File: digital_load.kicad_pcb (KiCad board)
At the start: 2 copper layers, 100 x 95 mm, 77 parts, among them J1 Conn_01x02, J10 Conn_PIC_ICSP_ICD, J2 Conn_01x02, J3 Conn_01x04, J4 Conn_01x04, J5 USB_C_Receptacle_USB2.0, Q20 BSB280N15NZ3, Q21 Q_NMOS_DGS, Q22 Q_NMOS_DGS, Q23 Q_NMOS_DGS, SW30 PEC11R, U10 PIC18F24K42, U20 LM358, U21 LM4040DBZ-2.0, U30 Adafruit_PiOLED, U40 LP2951-3.3_SOIC, U60 FT232RL, U61 CP2102N-Axx-xQFN28, U62 CH340C

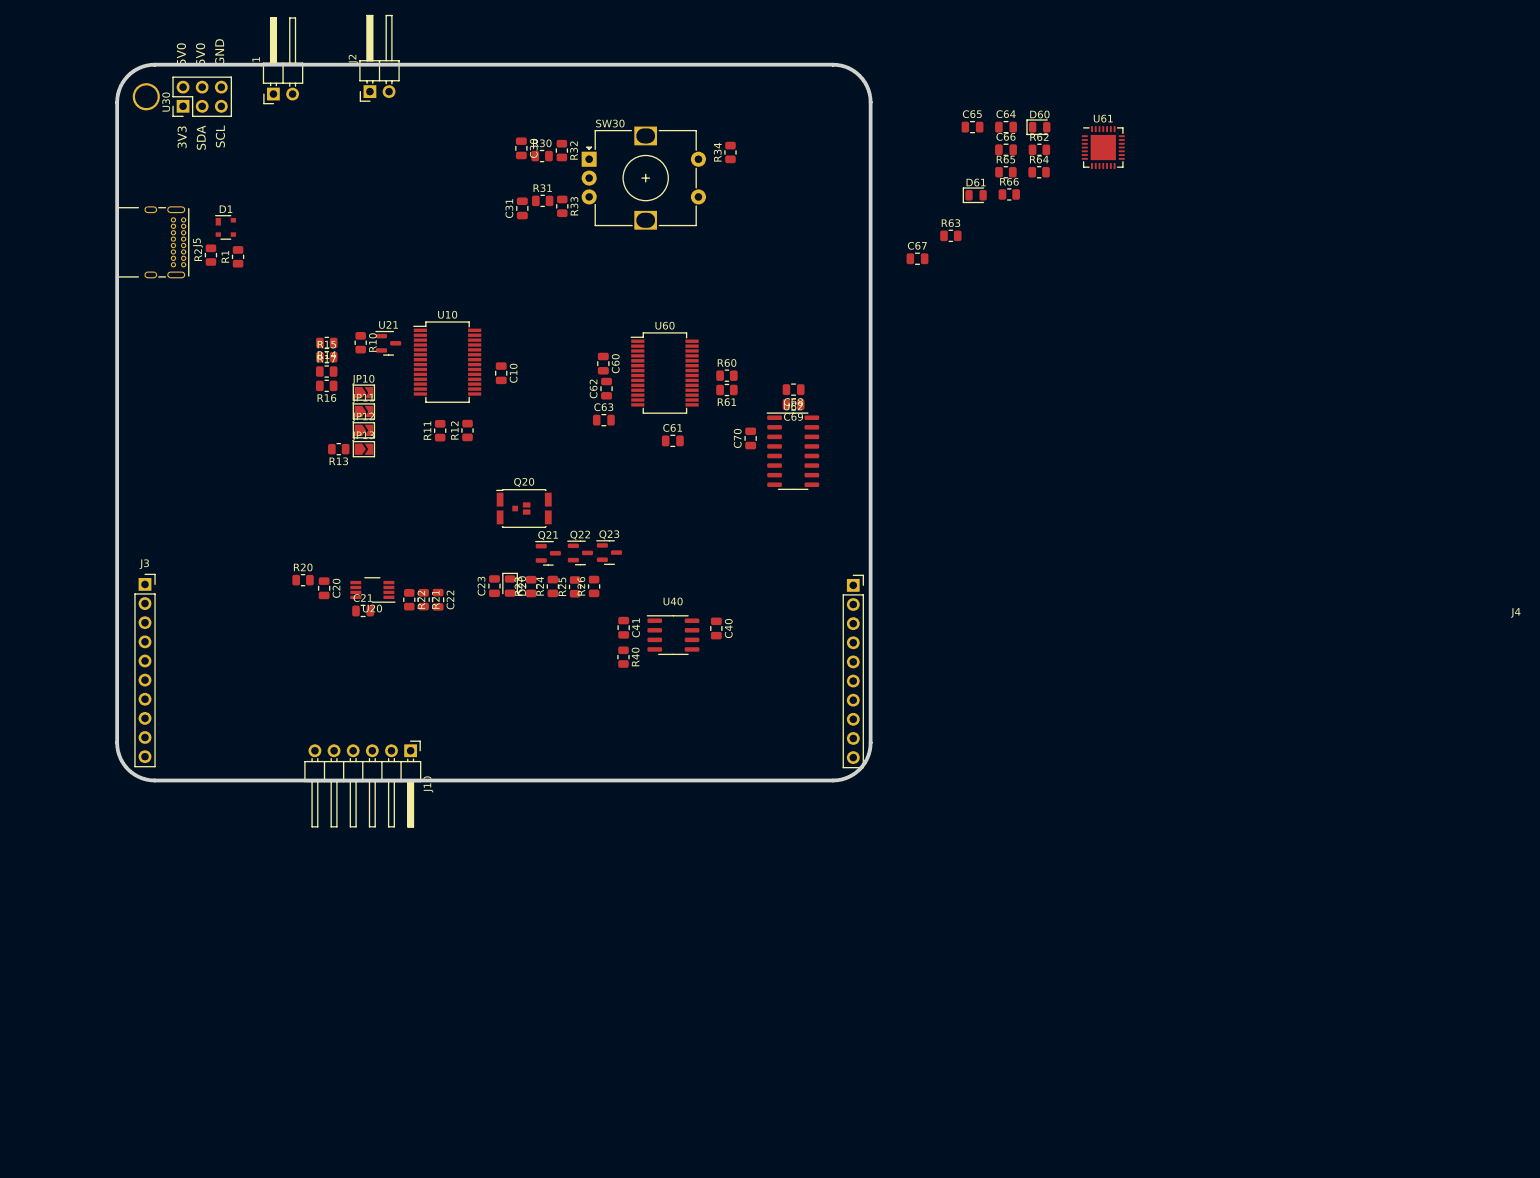
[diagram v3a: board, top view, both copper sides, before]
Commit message: WIP PCB Routing + Add load voltage measure
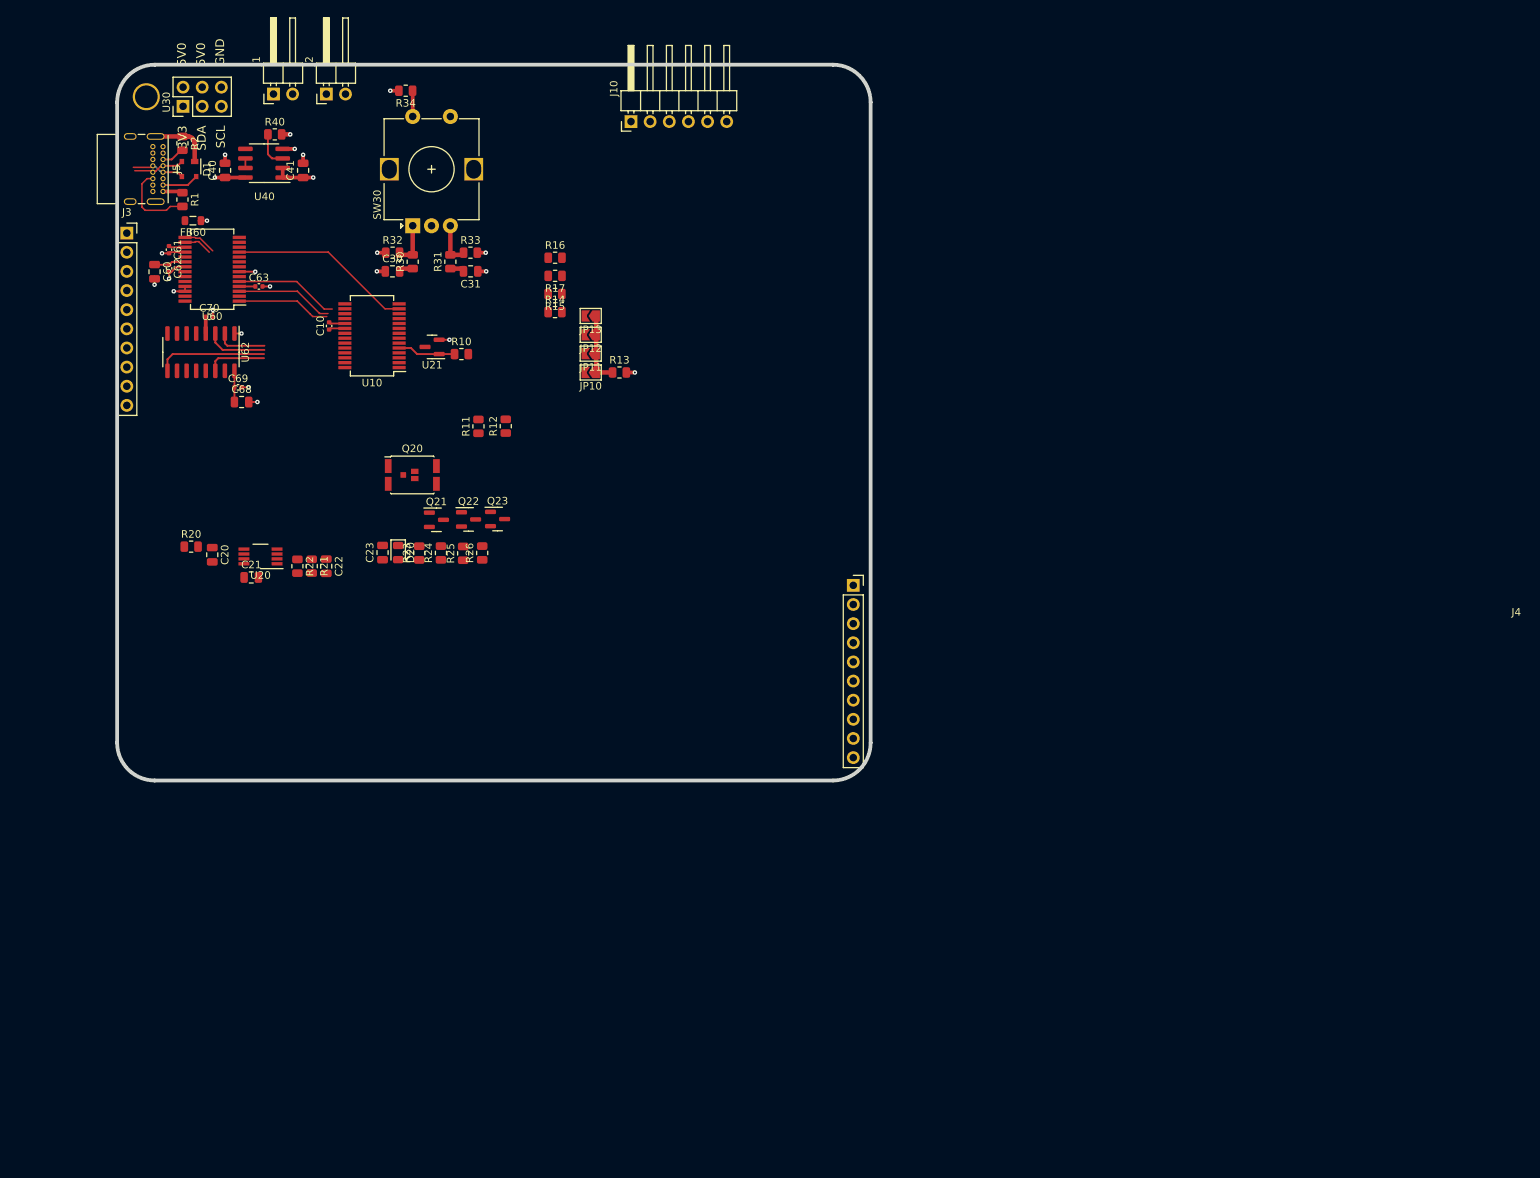
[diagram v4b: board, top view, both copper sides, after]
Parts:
- removed C64, C65: 100n, Capacitor_SMD:C_0805_2012Metric
- removed C66, C67: 4.7u, Capacitor_SMD:C_0805_2012Metric
- removed D60, D61: LED, LED_SMD:LED_0805_2012Metric
- removed R60: 4.7k, Resistor_SMD:R_0805_2012Metric
- removed R61, R65, R66: 10k, Resistor_SMD:R_0805_2012Metric
- removed R62: 22.1k, Resistor_SMD:R_0805_2012Metric
- removed R63: 47.5k, Resistor_SMD:R_0805_2012Metric
- removed R64: 1k, Resistor_SMD:R_0805_2012Metric
- removed U61: CP2102N-Axx-xQFN28, Package_DFN_QFN:QFN-28-1EP_5x5mm_P0.5mm_EP3.35x3.35mm
- added FB60: FerriteBead, Inductor_SMD:L_0805_2012Metric, F.Cu at (110.1, 55.7)
- C10, C61, C62, C63, C69, C70: footprint Capacitor_SMD:C_0805_2012Metric -> Capacitor_SMD:C_0402_1005Metric
- moved C40 89.1 mm to (114.3, 49.0), turned to 90 degrees
- moved J10 88.5 mm to (168.2, 42.5), turned to 90 degrees
- moved R40 83.4 mm to (120.9, 44.2), turned to 0 degrees
- moved U40 82.9 mm to (119.5, 48.1), turned to 180 degrees
- moved U62 79.7 mm to (111.1, 73.2), turned to -90 degrees
- moved C41 74.1 mm to (124.7, 49.0), turned to 90 degrees
- moved C69 73.8 mm to (116.0, 77.8), turned to 0 degrees
- moved C70 73.6 mm to (112.2, 68.5), turned to 0 degrees
- moved C68 73.3 mm to (116.5, 79.8), turned to 0 degrees
- moved C61 71.5 mm to (106.9, 59.5), turned to -90 degrees
- moved U60 61.6 mm to (112.6, 62.1), turned to 180 degrees
- moved C60 60.8 mm to (105.0, 62.5)
- moved C62 60.2 mm to (106.9, 62.0), turned to -90 degrees
- moved C63 49.1 mm to (118.8, 64.4)
- moved J3 46.7 mm to (101.3, 57.4)
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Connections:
- C60 pad 1: +5V -> Net-(C60-Pad1)
- C62 pad 1: +5V -> Net-(C60-Pad1)
- C63 pad 1: +5V -> Net-(C60-Pad1)
- U60 pad 19: Net-(R60-Pad1) -> unconnected-(U60-Pad19)
- U60 pad 20: +5V -> Net-(C60-Pad1)
- U60 pad 4: +5V -> Net-(C60-Pad1)
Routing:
- net /microcontroller/UART.RTS: track 0.00 -> 39.0 mm
- net GND: track 0.00 -> 38.1 mm, vias 0 -> 17
- net /microcontroller/UART.TX: track 0.00 -> 22.0 mm
- net /microcontroller/UART.CTS: track 0.00 -> 20.9 mm
- net /microcontroller/UART.RX: track 0.00 -> 19.1 mm
- net +5V: track 0.00 -> 14.2 mm, vias 0 -> 2
- net +3V3: track 0.00 -> 12.0 mm, vias 0 -> 5
- net /Connectors/USB2.0.D+: track 0.00 -> 11.3 mm
- net /Connectors/USB2.0.D-: track 0.00 -> 10.9 mm
- net Net-(J5-PadB5): track 0.00 -> 10.6 mm
- net Net-(JP10-Pad1): track 0.00 -> 9.68 mm
- net /microcontroller/2.048V: track 0.00 -> 7.70 mm
- net Net-(C60-Pad1): track 0.00 -> 5.95 mm
- net Net-(R31-Pad2): track 0.00 -> 5.74 mm
- net Net-(R30-Pad2): track 0.00 -> 5.73 mm
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- added copper zone on In1.Cu, net GND
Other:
- copper layers 2 -> 4
- rule pad_to_mask_clearance: 0 -> 0.1

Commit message: WIP PCB Routing
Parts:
- removed J2: Conn_01x02, Connector_PinHeader_2.54mm:PinHeader_1x02_P2.54mm_Horizontal
- added C24: 100n, Capacitor_SMD:C_0402_1005Metric, F.Cu at (112.6, 137.9)
- added R27: 5M, Resistor_SMD:R_0805_2012Metric, F.Cu at (117.2, 145.8)
- added R28: 50k, Resistor_SMD:R_0805_2012Metric, F.Cu at (112.8, 145.8)
- added R29: 10k, Resistor_SMD:R_0805_2012Metric, F.Cu at (115.9, 137.7)
- added U21: LM358, Package_SO:VSSOP-8_3.0x3.0mm_P0.65mm, F.Cu at (110.9, 140.7)
- C21: value C_Small -> 100n; footprint Capacitor_SMD:C_0805_2012Metric -> Capacitor_SMD:C_0402_1005Metric
- J10: footprint Connector_PinHeader_2.54mm:PinHeader_1x06_P2.54mm_Horizontal -> Connector_PinHeader_2.54mm:PinHeader_1x06_P2.54mm_Vertical
- JP10, JP11, JP12, JP13: value SolderJumper_2_Open -> SB
- Q20: value BSB280N15NZ3 -> IPA60R800CE; footprint Package_DirectFET:DirectFET_MZ -> Package_TO_SOT_THT:TO-220-3_Horizontal_TabDown
- moved J1 132.0 mm to (129.2, 170.6), turned to -90 degrees
- moved J10 64.2 mm to (118.1, 82.7)
- moved R16 55.7 mm to (116.0, 97.1), turned to 180 degrees
- moved Q23 53.9 mm to (131.2, 145.7), turned to 180 degrees
- moved R17 52.7 mm to (116.0, 94.7), turned to 0 degrees
- moved Q22 51.6 mm to (135.0, 145.6), turned to 180 degrees
- moved Q21 50.3 mm to (139.3, 145.6), turned to 180 degrees
- moved R15 49.9 mm to (116.0, 92.3), turned to 0 degrees
- moved J4 49.5 mm to (148.2, 102.4)
- moved R34 49.4 mm to (132.8, 87.5), turned to -90 degrees
- moved R14 47.5 mm to (116.0, 89.9), turned to 180 degrees
- moved JP13 46.9 mm to (132.7, 104.2), turned to -90 degrees
- moved R40 46.4 mm to (129.5, 89.9), turned to -90 degrees
- moved J3 45.0 mm to (101.8, 102.4)
- moved C61 45.0 mm to (104.7, 104.5)
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- renumbered U21 to U11
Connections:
- Q20 pad 1: /Connectors/load_in -> Net-(Q20-Pad1)
- Q20 pad 2: Net-(Q20-Pad2) -> /Connectors/load_in
- U10 pad 10: /microcontroller/I2C_A1 -> /microcontroller/I2C_A3
- U10 pad 11: /microcontroller/I2C_A2 -> /Display_Encoder/ENC.B
- U10 pad 12: /microcontroller/I2C_A3 -> /Display_Encoder/ENC.A
- U10 pad 13: /microcontroller/UART.RTS -> /Display_Encoder/select
- U10 pad 16: /microcontroller/UART.TX -> /microcontroller/3V3_sense
- U10 pad 17: /microcontroller/UART.CTS -> /microcontroller/5V_sense
- U10 pad 18: /microcontroller/UART.RX -> /microcontroller/UART.RTS
- U10 pad 21: /Display_Encoder/ENC.B -> /microcontroller/UART.TX
- U10 pad 22: /load_control/range.1ma -> /microcontroller/UART.CTS
- U10 pad 23: /load_control/range.100ma -> /microcontroller/UART.RX
- U10 pad 24: /load_control/range.10a -> /load_control/range.100ma
- U10 pad 3: /Display_Encoder/select -> unconnected-(U10-Pad3)
- U10 pad 4: /Display_Encoder/ENC.A -> unconnected-(U10-Pad4)
- U10 pad 6: /microcontroller/3V3_sense -> /microcontroller/I2C_A0
- U10 pad 7: /microcontroller/5V_sense -> /microcontroller/I2C_A1
- U10 pad 9: /microcontroller/I2C_A0 -> /microcontroller/I2C_A2
- U20 pad 7: Net-(Q20-Pad2) -> Net-(Q20-Pad1)
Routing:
- net /Connectors/USB2.0.D-: track 10.9 -> 37.4 mm
- net /Connectors/USB2.0.D+: track 11.3 -> 36.6 mm
- net /Display_Encoder/select: track 3.42 -> 28.2 mm
- net /Display_Encoder/ENC.B: track 1.91 -> 21.7 mm
- net /load_control/current_measure: track 0.00 -> 19.1 mm
- net /microcontroller/UART.RTS: track 39.0 -> 21.9 mm
- net /microcontroller/3V3_sense: track 0.00 -> 16.1 mm
- net /microcontroller/I2C_A0: track 0.00 -> 15.3 mm
- net Net-(R31-Pad2): track 5.74 -> 20.1 mm
- net /Display_Encoder/ENC.A: track 1.88 -> 15.1 mm
- net GND: track 38.1 -> 51.0 mm, vias 17 -> 18
- net /microcontroller/I2C_A1: track 0.00 -> 12.2 mm
- net /microcontroller/5V_sense: track 0.00 -> 12.0 mm
- net /microcontroller/I2C_A2: track 0.00 -> 9.06 mm
- net Net-(C22-Pad1): track 0.00 -> 7.01 mm
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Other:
- board size 100 x 95 mm -> 50 x 50 mm
- board text added: "A0"
- board text added: "A1"
- board text added: "A2"
- board text added: "A3"

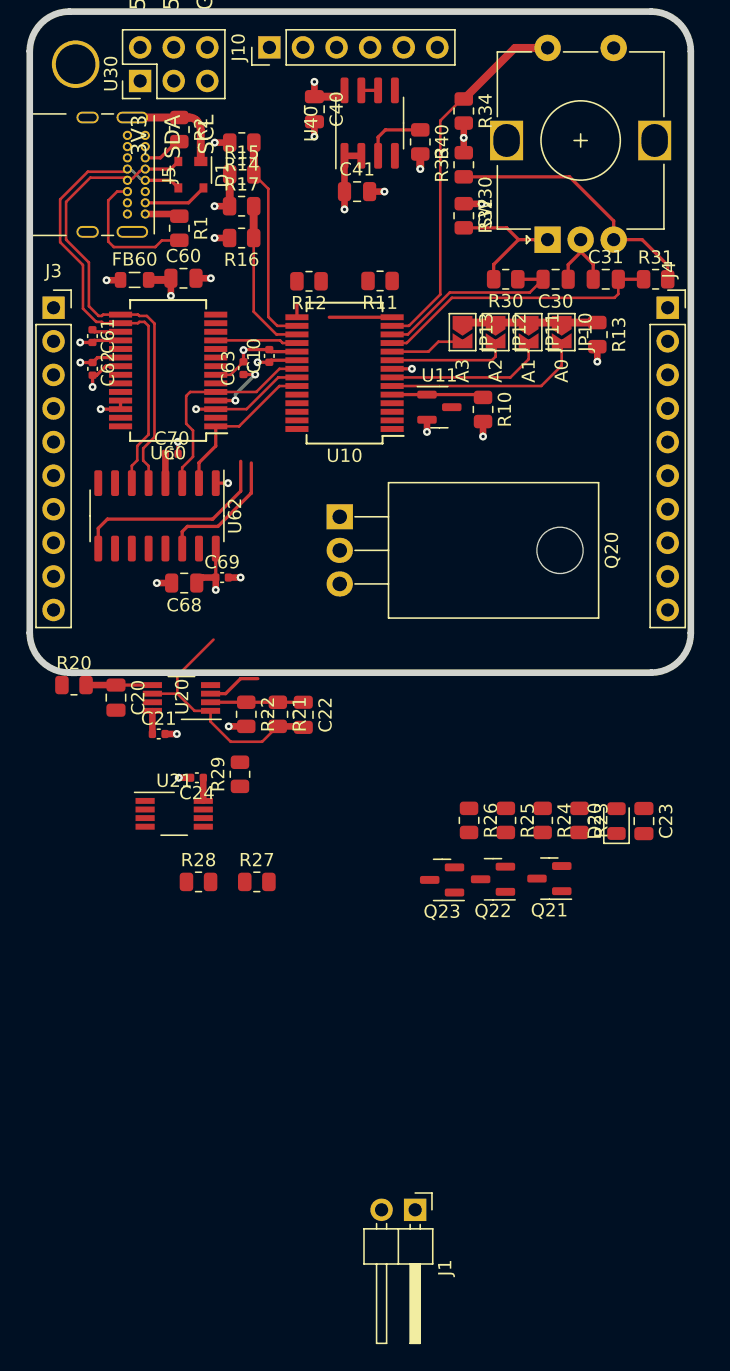
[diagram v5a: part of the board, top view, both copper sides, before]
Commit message: Add heatsink, among other things
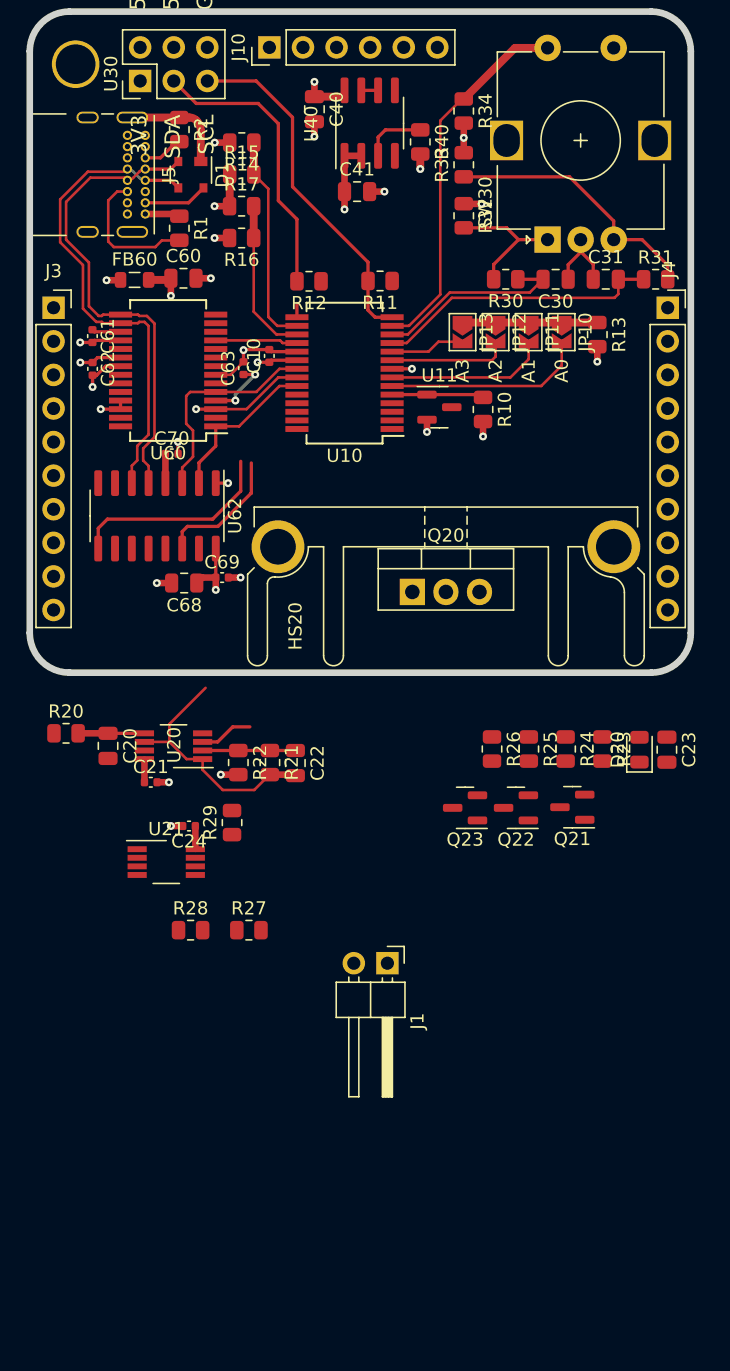
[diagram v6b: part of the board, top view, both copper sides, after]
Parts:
- added HS20: Heatsink_Pad, 0_Heatsink:Heatsink_ASSMANN_WSW_V6560W, F.Cu at (131.5, 120.5)
- Q20: footprint Package_TO_SOT_THT:TO-220-3_Horizontal_TabDown -> Package_TO_SOT_THT:TO-220-3_Vertical
- moved J1 18.8 mm to (127.0, 152.0)
- moved Q20 7.90 mm to (128.9, 123.9), turned to 0 degrees
- moved Q23 5.72 mm to (132.9, 140.2)
- moved C23 5.67 mm to (148.2, 135.8)
- moved D20 5.67 mm to (146.1, 135.8)
- moved Q22 5.67 mm to (136.8, 140.2)
- moved R23 5.67 mm to (143.3, 135.8)
- moved R24 5.67 mm to (140.5, 135.8)
- moved R25 5.67 mm to (137.7, 135.8)
- moved R26 5.67 mm to (135.0, 135.8)
- moved Q21 5.67 mm to (141.0, 140.2)
- moved C20 3.70 mm to (105.9, 135.5)
- moved C22 3.70 mm to (120.1, 136.8)
- moved R21 3.70 mm to (118.2, 136.8)
- moved R29 3.70 mm to (115.3, 141.3)
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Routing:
- net /Connectors/I2C.SCL: track 4.75 -> 26.6 mm
- net /Connectors/I2C.SDA: track 1.05 -> 22.8 mm
